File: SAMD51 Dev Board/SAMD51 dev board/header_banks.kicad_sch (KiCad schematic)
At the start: 23 parts, among them J10 Conn_02x16_Top_Bottom, J11 Conn_01x07, J12 Conn_01x05, J13 Conn_01x08, J14 Conn_02x16_Top_Bottom, J15 Conn_01x05, J16 Conn_01x06, J17 Conn_01x10, J4 Conn_01x07, J5 Conn_02x16_Top_Bottom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

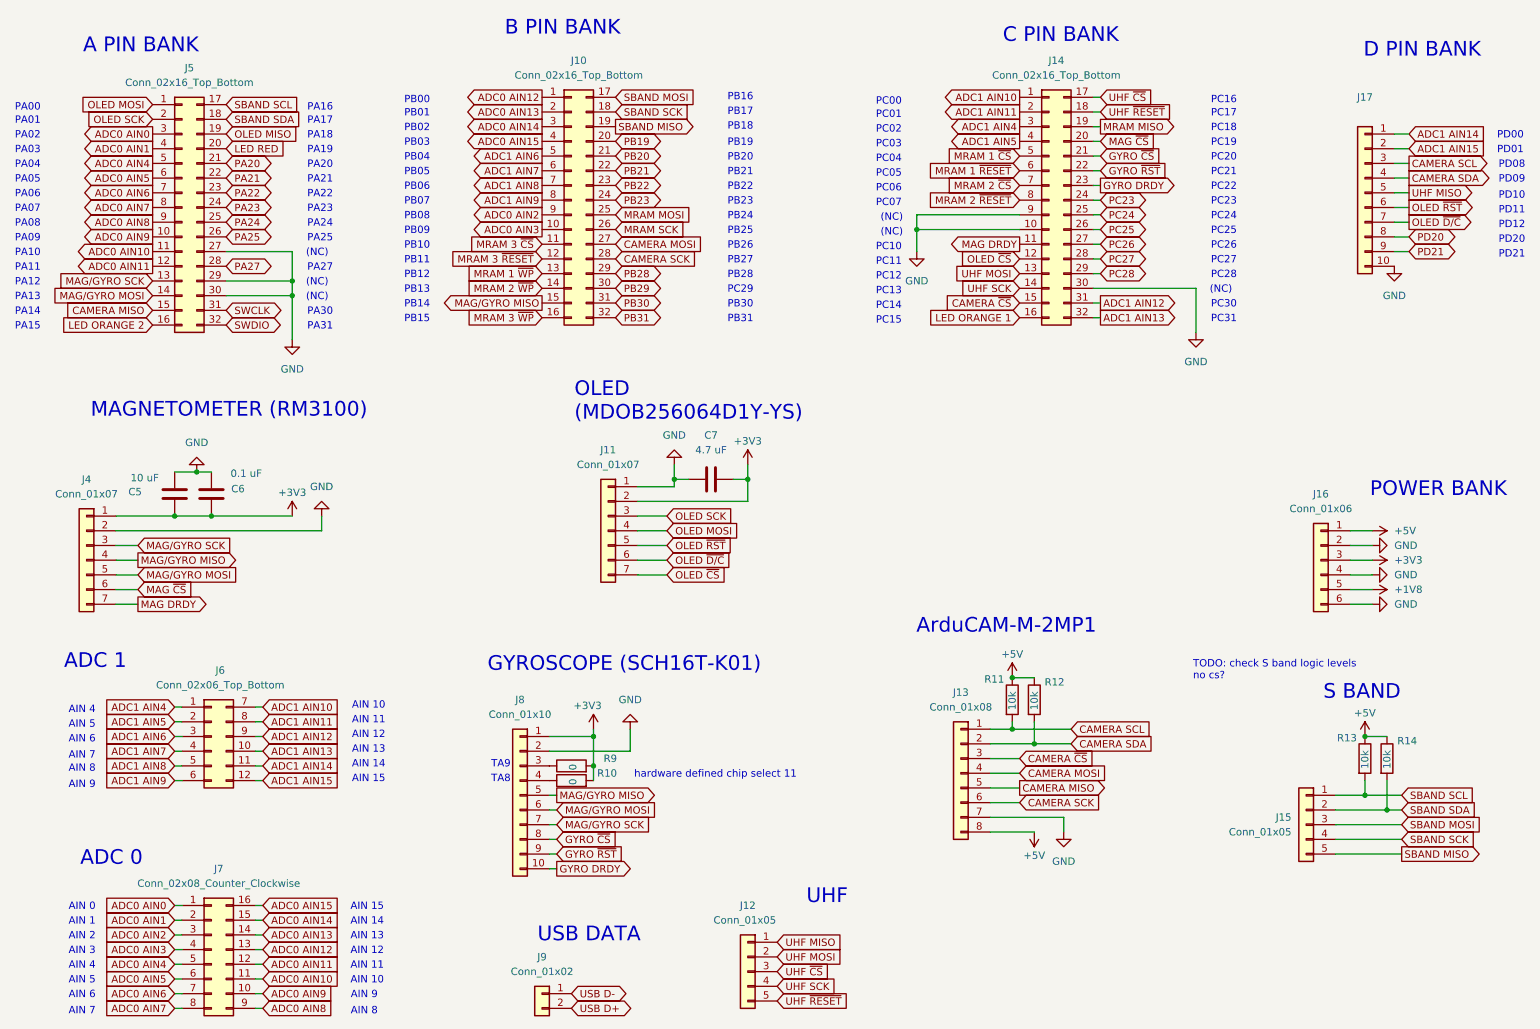
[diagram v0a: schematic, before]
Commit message: routed samd51 breakout
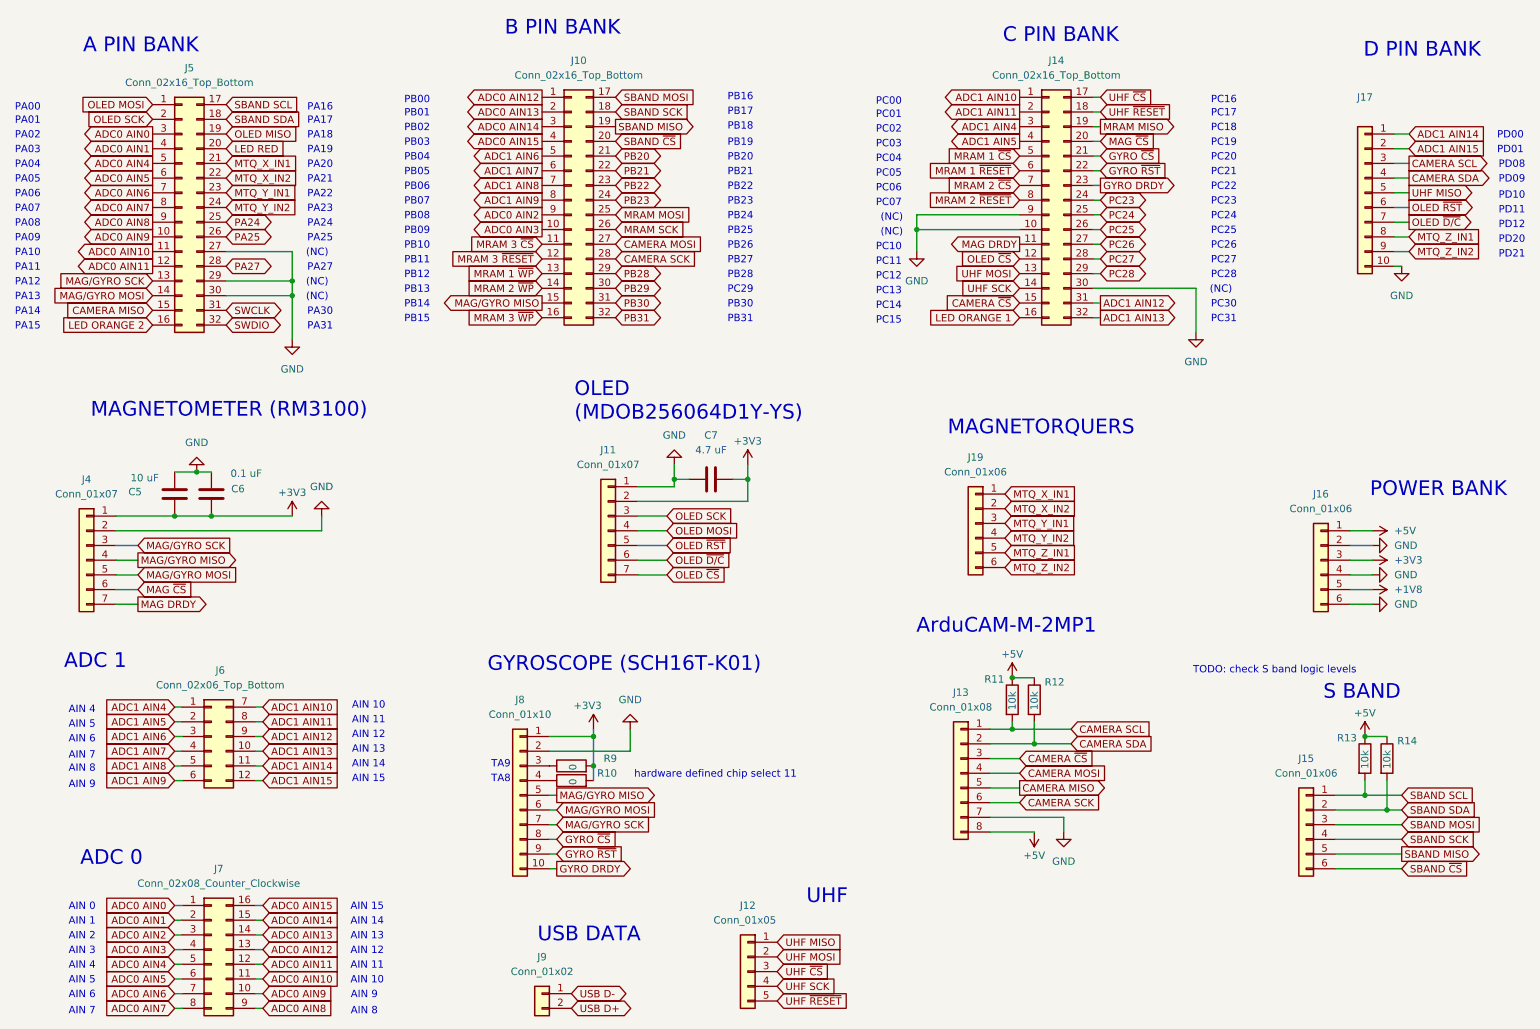
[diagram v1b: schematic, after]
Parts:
- removed J15: Conn_01x05, Connector_PinSocket_2.54mm:PinSocket_1x05_P2.54mm_Vertical, symbol Connector_Generic:Conn_01x05
- added J15, J19: Conn_01x06, Connector_PinSocket_2.54mm:PinSocket_1x06_P2.54mm_Vertical, symbol Connector_Generic:Conn_01x06
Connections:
- net SBAND MISO: now also J15.5 (Pin_5)
- net SBAND MOSI: now also J15.3 (Pin_3)
- net SBAND SCK: now also J15.4 (Pin_4)
- net SBAND SCL: now also J15.1 (Pin_1)
- net SBAND SDA: now also J15.2 (Pin_2)
- net PA20 renamed MTQ_X_IN1
- net MTQ_X_IN1: now also J19.1 (Pin_1)
- net PA21 renamed MTQ_X_IN2
- net MTQ_X_IN2: now also J19.2 (Pin_2)
- net PA22 renamed MTQ_Y_IN1
- net MTQ_Y_IN1: now also J19.3 (Pin_3)
- net PA23 renamed MTQ_Y_IN2
- net MTQ_Y_IN2: now also J19.4 (Pin_4)
- net PB19 renamed SBAND ~{CS}
- net SBAND ~{CS}: now also J15.6 (Pin_6)
- net PD20 renamed MTQ_Z_IN1
- net MTQ_Z_IN1: now also J19.5 (Pin_5)
- net PD21 renamed MTQ_Z_IN2
- net MTQ_Z_IN2: now also J19.6 (Pin_6)
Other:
- note added: "MAGNETORQUERS"
- note added: "TODO: check S band logic levels"
- note removed: "TODO: check S band logic levels no cs?"
